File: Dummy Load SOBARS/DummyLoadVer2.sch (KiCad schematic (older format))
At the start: 22 parts, among them J1 Power, J2 Batt Monitor, J4 To Dummy Load 50 Ohms

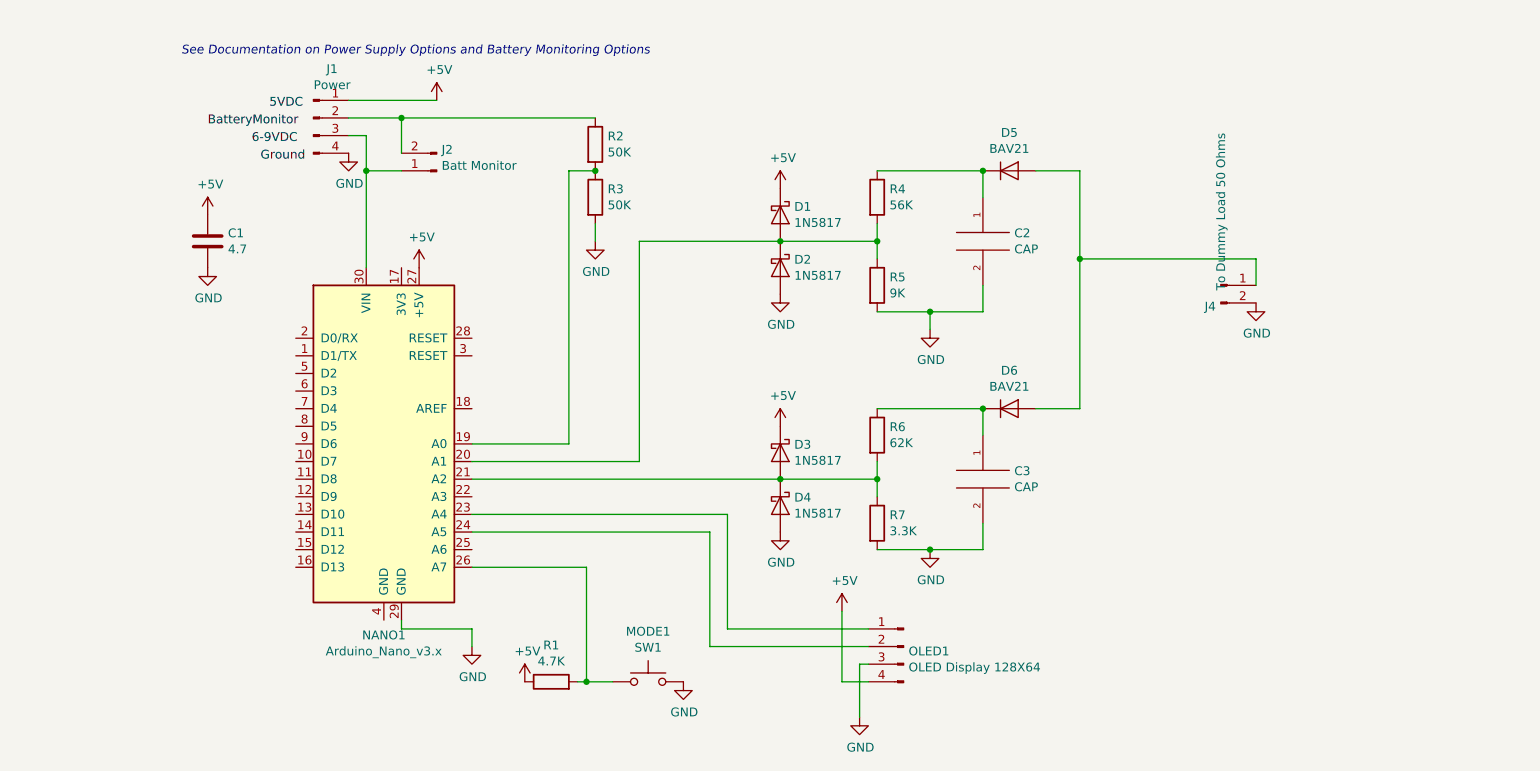
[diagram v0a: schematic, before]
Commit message: Fix Mode Pin Digital Minor adjustments
Clean up some traces
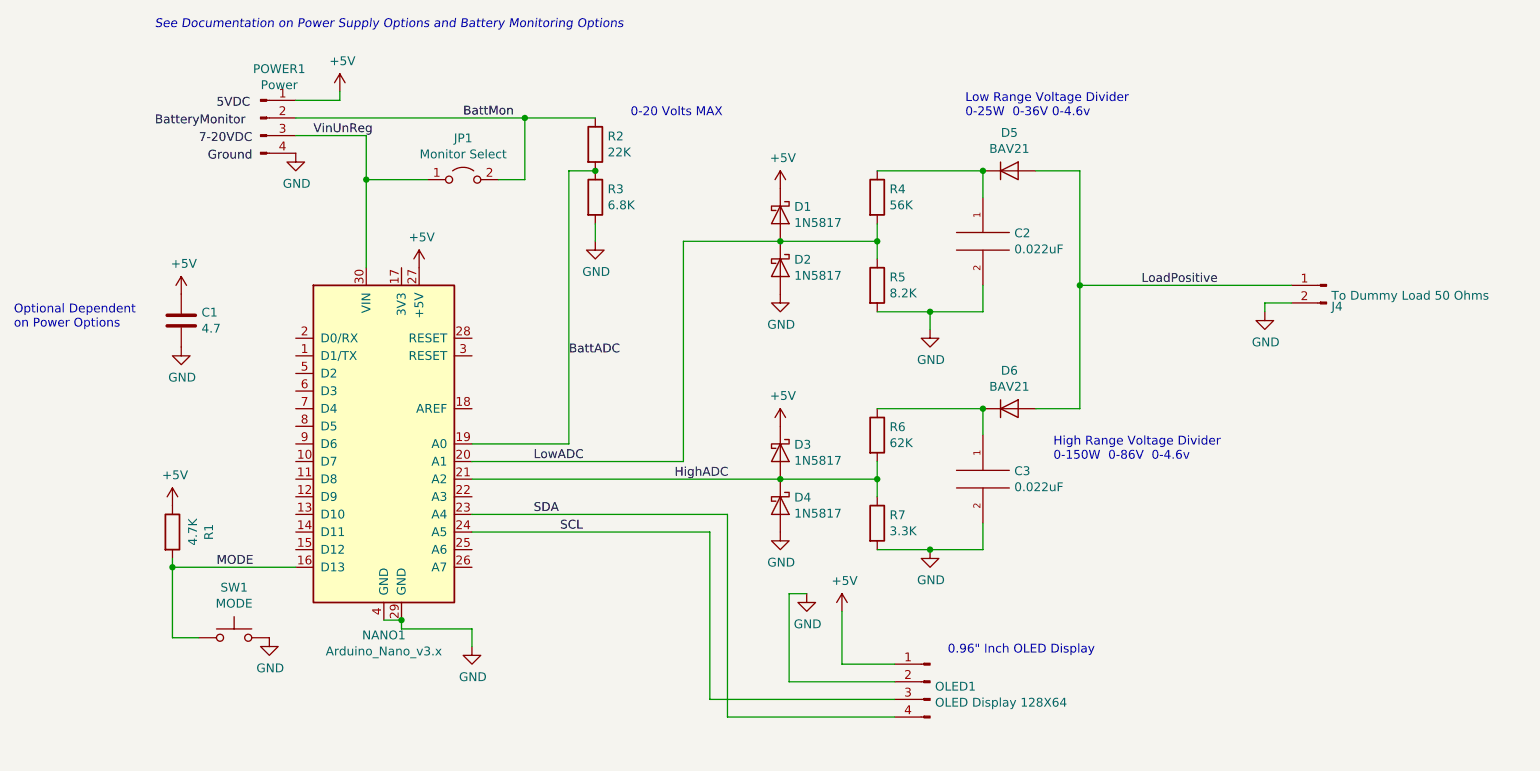
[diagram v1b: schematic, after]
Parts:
- removed J2: Batt Monitor, Connector_PinSocket_2.54mm:PinSocket_1x02_P2.54mm_Vertical, symbol Connector:Conn_01x02_Male
- added JP1: Monitor Select, Connector_PinSocket_2.54mm:PinSocket_1x02_P2.54mm_Vertical, symbol Jumper:Jumper_2_Open
- C2, C3: value CAP -> 0.022uF
- J4: value To Dummy Load 50 Ohms -> To Dummy Load 50 Ohms
- R2: value 50K -> 22K
- R3: value 50K -> 6.8K
- R5: value 9K -> 8.2K
- SW1: renamed from MODE1; value SW1 -> MODE
- renumbered J1 to POWER1
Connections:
- net +5V: now also OLED1.1 (Pin_1); no longer OLED1.4 (Pin_4)
- net GND: now also NANO1.4 (GND), OLED1.2 (Pin_2); no longer OLED1.3 (Pin_3)
- net MODE: now reaches NANO1.16 (D13)
- net MODE: now also R1.2, SW1.1
- net BattADC: now reaches NANO1.19 (A0), R2.2, R3.1
- net LowADC: now reaches D1.2 (A), D2.1 (K), NANO1.20 (A1), R4.2, R5.1
- net HighADC: now reaches D3.2 (A), D4.1 (K), NANO1.21 (A2), R6.2, R7.1
- net SDA: now reaches NANO1.23 (A4)
- net SDA: now also OLED1.4 (Pin_4); no longer OLED1.1 (Pin_1)
- net SCL: now reaches NANO1.24 (A5)
- net SCL: now also OLED1.3 (Pin_3); no longer OLED1.2 (Pin_2)
- net VinUnReg: now reaches NANO1.30 (VIN), POWER1.3 (Pin_3)
- net VinUnReg: now also JP1.1 (A)
- net LoadPositive: now reaches D5.2 (A), D6.2 (A), J4.1 (Pin_1)
- net BattMon: now reaches POWER1.2 (Pin_2), R2.1
- net BattMon: now also JP1.2 (B)
- now unconnected: NANO1.26 (A7)
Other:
- note added: "0-20 Volts MAX"
- note added: "0.96" Inch OLED Display"
- note added: "High Range Voltage Divider \n0-150W 0-86V 0-4.6v"
- note added: "Low Range Voltage Divider \n0-25W 0-36V 0-4.6v"
- note added: "Optional Dependent \non Power Options"
- moved on the sheet: C1, J4, OLED1, POWER1, R1, SW1
